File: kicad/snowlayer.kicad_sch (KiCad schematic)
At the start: 102 parts, among them P1 USB_C_Plug_USB2.0, P2 USB_C_Plug_USB2.0, P3 USB_C_Plug_USB2.0, SW1 SW_Push, SW10 SW_Push, SW11 SW_Push, SW12 SW_Push, SW13 SW_Push, SW14 SW_Push, SW15 SW_Push, SW16 SW_Push, SW17 SW_Push, SW18 SW_Push, SW19 SW_Push, SW2 SW_Push, SW20 SW_Push, SW21 SW_Push, SW22 SW_Push, SW23 SW_Push, SW24 SW_Push, SW25 SW_Push, SW26 SW_Push, SW27 SW_Push, SW28 SW_Push, SW29 SW_Push, SW3 SW_Push, SW30 SW_Push, SW31 SW_Push, SW32 SW_Push, SW33 SW_Push, SW34 SW_Push, SW35 SW_Push, SW36 SW_Push, SW37 SW_Push, SW38 SW_Push, SW39 SW_Push, SW4 SW_Push, SW40 SW_Push, SW41 SW_Push, SW5 SW_Push, SW50 SW_Push, SW51 SW_Push, SW6 SW_Push, SW7 SW_Push, SW8 SW_Push, SW9 SW_Push, U1 CH32X035DS0

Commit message: feat: finish BOM, change out diodes + major rerouting, new journal entry
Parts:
- D1, D10, D11, D12, D13, D14, D15, D16, D17, D18, D19, D2, D20, D21, D22, D23, D24, D25, D26, D27, D28, D29, D3, D30, D31, D32, D33, D34, D35, D36, D37, D38, D39, D4, D40, D5, D50, D51, D6, D7, D8, D9: footprint Diode_SMD:D_SMA-SMB_Universal_Handsoldering -> Diode_SMD:D_SOD-123
- R3: value 1k -> 1kO

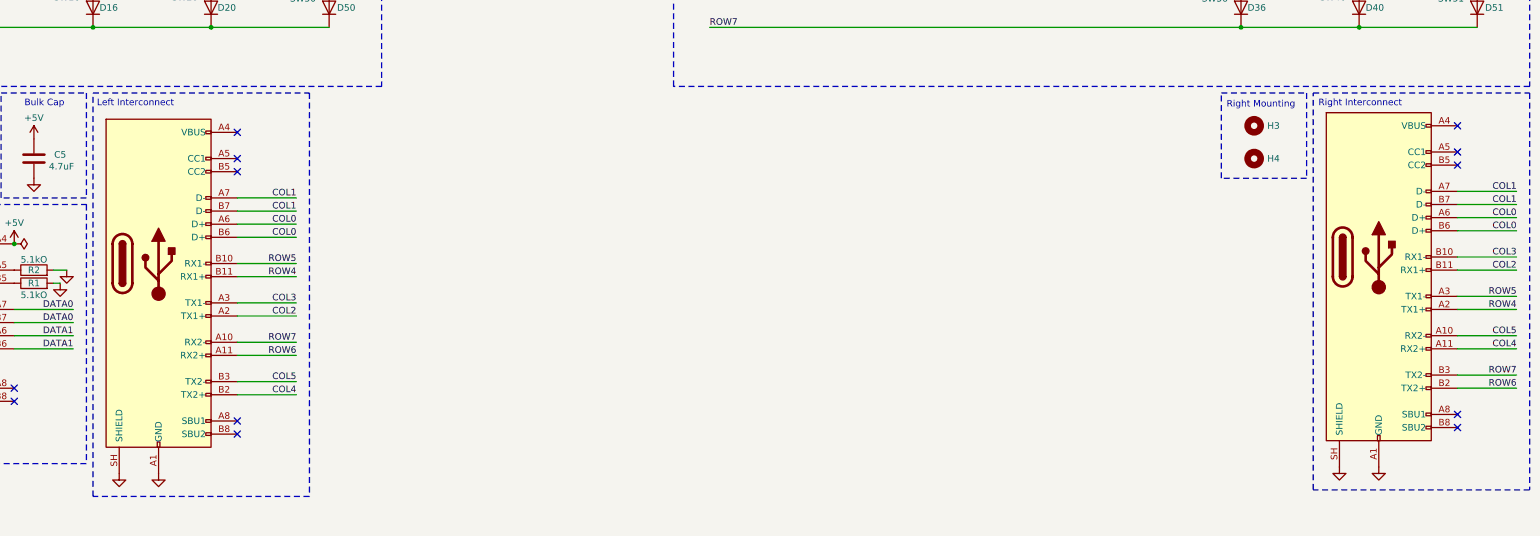
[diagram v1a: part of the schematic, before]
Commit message: feat: new journal, better components
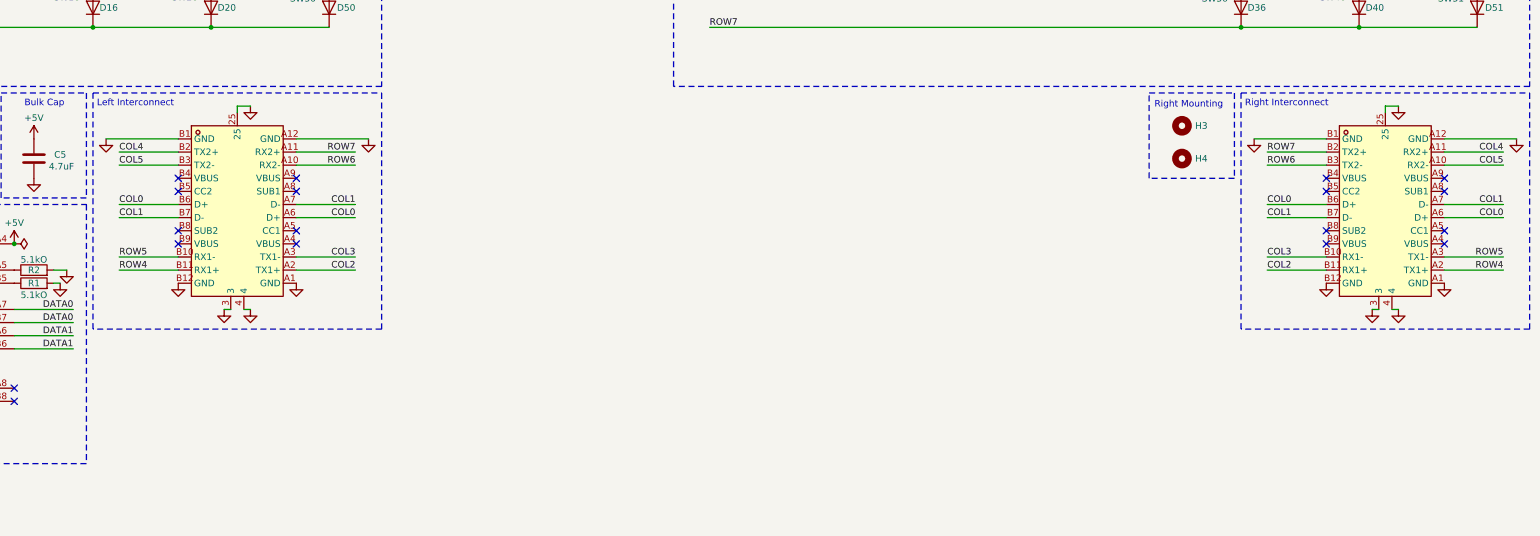
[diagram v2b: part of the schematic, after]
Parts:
- removed P1, P2: USB_C_Plug_USB2.0, Connector_USB:USB_C_Receptacle_Molex_105450-0101, symbol Connector:USB_C_Receptacle
- added USB1, USB2: TYPEC-24PIN_C53207800, snowlayer:USB-C-SMD_TYPE-C-24P-QT, symbol snowlayer:TYPEC-24PIN_C53207800
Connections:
- net COL0: now also USB1.A6 (D+), USB1.B6 (D+), USB2.A6 (D+), USB2.B6 (D+)
- net COL1: now also USB1.A7 (D-), USB1.B7 (D-), USB2.A7 (D-), USB2.B7 (D-)
- net COL2: now also USB1.A2 (TX1+), USB2.B11 (RX1+)
- net COL3: now also USB1.A3 (TX1-), USB2.B10 (RX1-)
- net COL4: now also USB1.B2 (TX2+), USB2.A11 (RX2+)
- net COL5: now also USB1.B3 (TX2-), USB2.A10 (RX2-)
- net GND: now also USB1.25, USB1.3, USB1.4, USB1.A1 (GND), USB1.A12 (GND), USB1.B1 (GND), USB1.B12 (GND), USB2.25, USB2.3, USB2.4, USB2.A1 (GND), USB2.A12 (GND), USB2.B1 (GND), USB2.B12 (GND)
- net ROW4: now also USB1.B11 (RX1+), USB2.A2 (TX1+)
- net ROW5: now also USB1.B10 (RX1-), USB2.A3 (TX1-)
- net ROW6: now also USB1.A10 (RX2-), USB2.B3 (TX2-)
- net ROW7: now also USB1.A11 (RX2+), USB2.B2 (TX2+)
- no-connect marks 21 -> 27
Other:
- moved on the sheet: H3, H4

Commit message: feat: new journal, update all file outputs, finish routing/case
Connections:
- net ROW4: now also U1.19 (PB8); no longer U1.18 (PB7)
- net ROW5: now also U1.18 (PB7); no longer U1.19 (PB8)
- net ROW6: now also U1.21 (PB10), USB1.A11 (RX2+), USB2.B2 (TX2+); no longer U1.20 (PB9), USB1.A10 (RX2-), USB2.B3 (TX2-)
- net ROW7: now also U1.20 (PB9), USB1.A10 (RX2-), USB2.B3 (TX2-); no longer U1.21 (PB10), USB1.A11 (RX2+), USB2.B2 (TX2+)
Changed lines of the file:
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@@
 		)
 	)
-	(label "ROW7"
+	(label "ROW6"
 		(at 353.06 118.11 0)
 		(effects
@@
 		)
 	)
-	(label "ROW6"
+	(label "ROW7"
 		(at 353.06 120.65 0)
 		(effects
@@
 		)
 	)
-	(label "ROW7"
+	(label "ROW6"
 		(at 176.53 118.11 180)
 		(effects
@@
 		)
 	)
-	(label "ROW7"
+	(label "ROW6"
 		(at 19.05 173.99 0)
 		(effects
@@
 		)
 	)
-	(label "ROW6"
+	(label "ROW7"
 		(at 176.53 120.65 180)
 		(effects
@@
 		)
 	)
-	(label "ROW4"
+	(label "ROW5"
 		(at 19.05 166.37 0)
 		(effects
@@
 		)
 	)
-	(label "ROW6"
+	(label "ROW7"
 		(at 19.05 171.45 0)
 		(effects
@@
 		)
 	)
-	(label "ROW5"
+	(label "ROW4"
 		(at 19.05 168.91 0)
 		(effects
